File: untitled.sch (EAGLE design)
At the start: 49 parts, among them J2 1x3 RA Female .1", J3 CORTEX_DEBUG_PTH, J4 USB-MICROB, Q1 BSS123

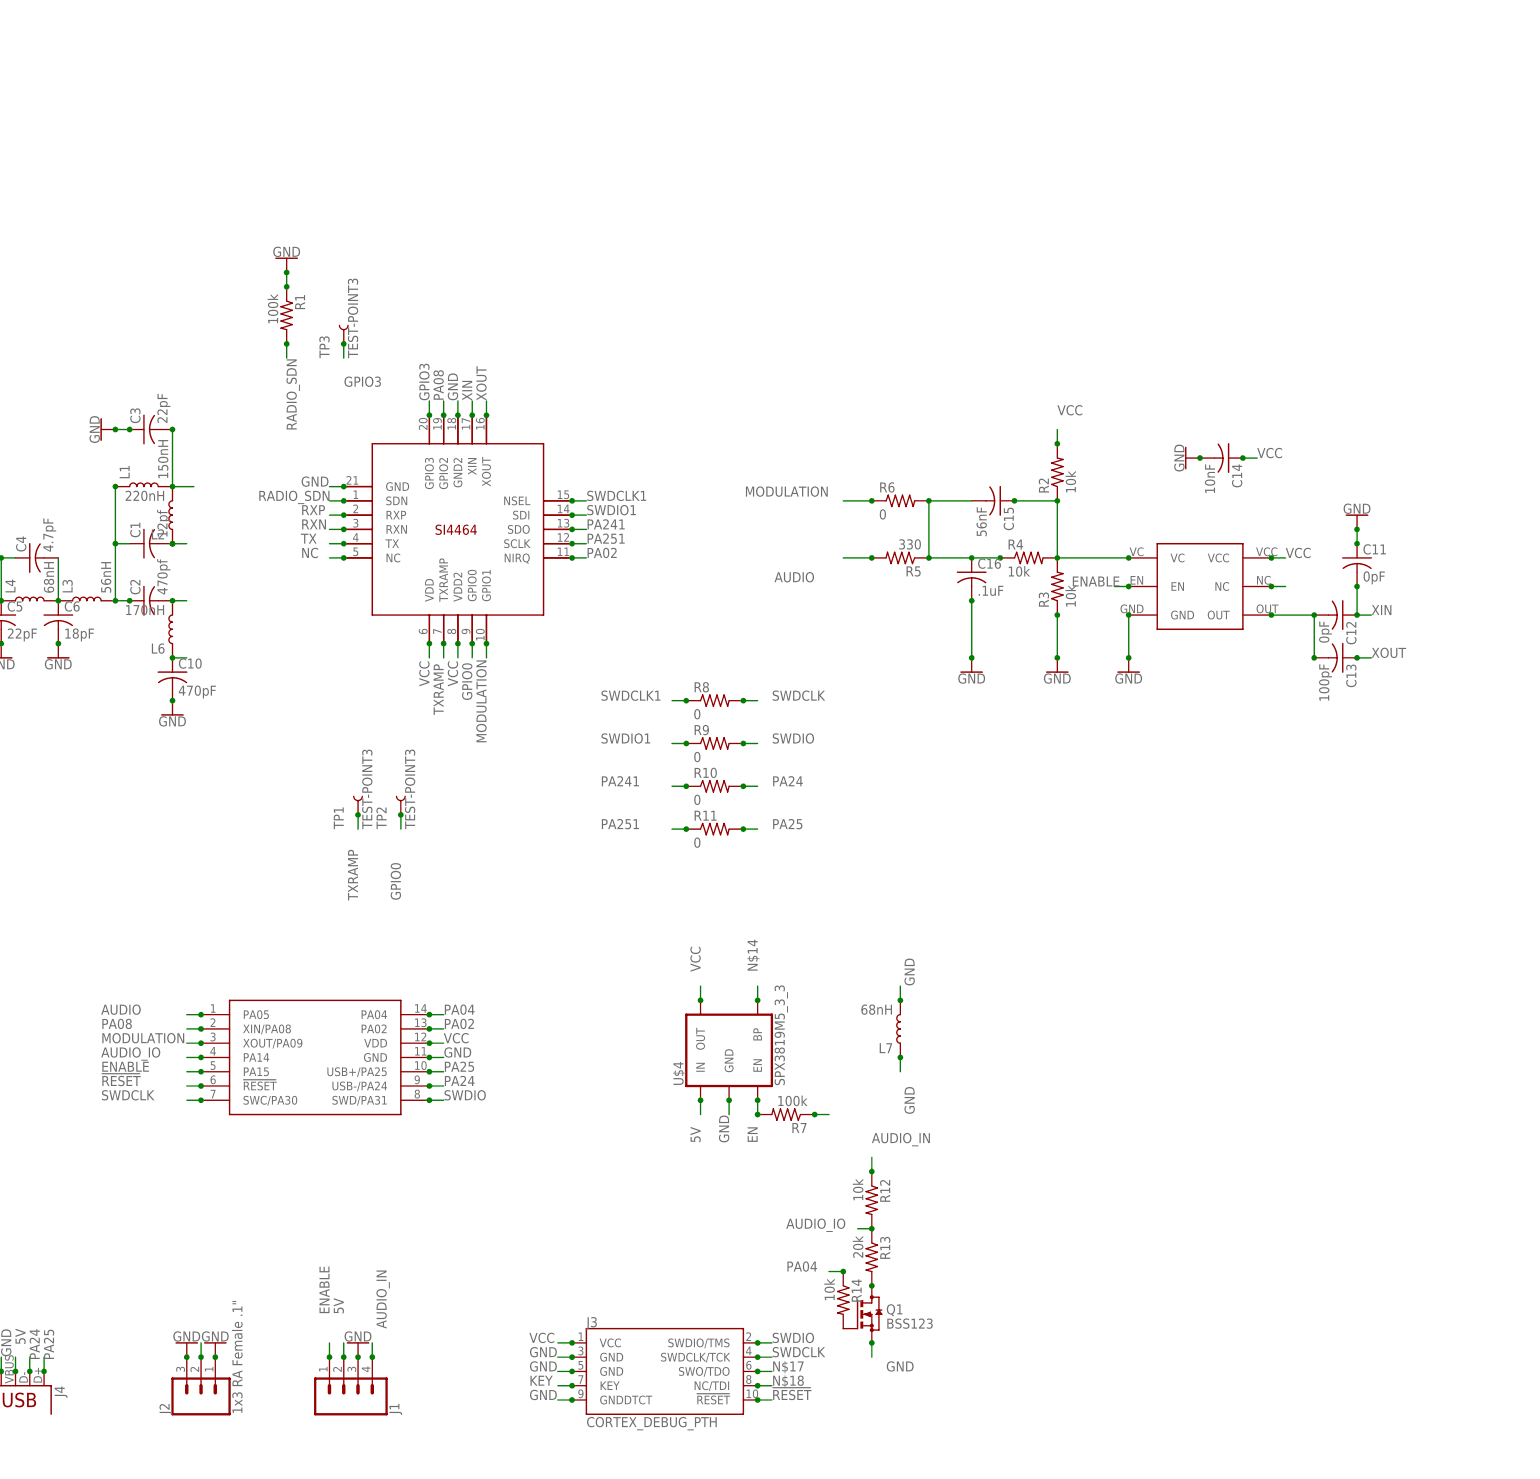
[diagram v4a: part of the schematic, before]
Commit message: changed audio input path
changed audio input to make the samd11c14 decode the audio and resend it to the VCO. Added fets to allow for i2c over enable and audio pins for future use.
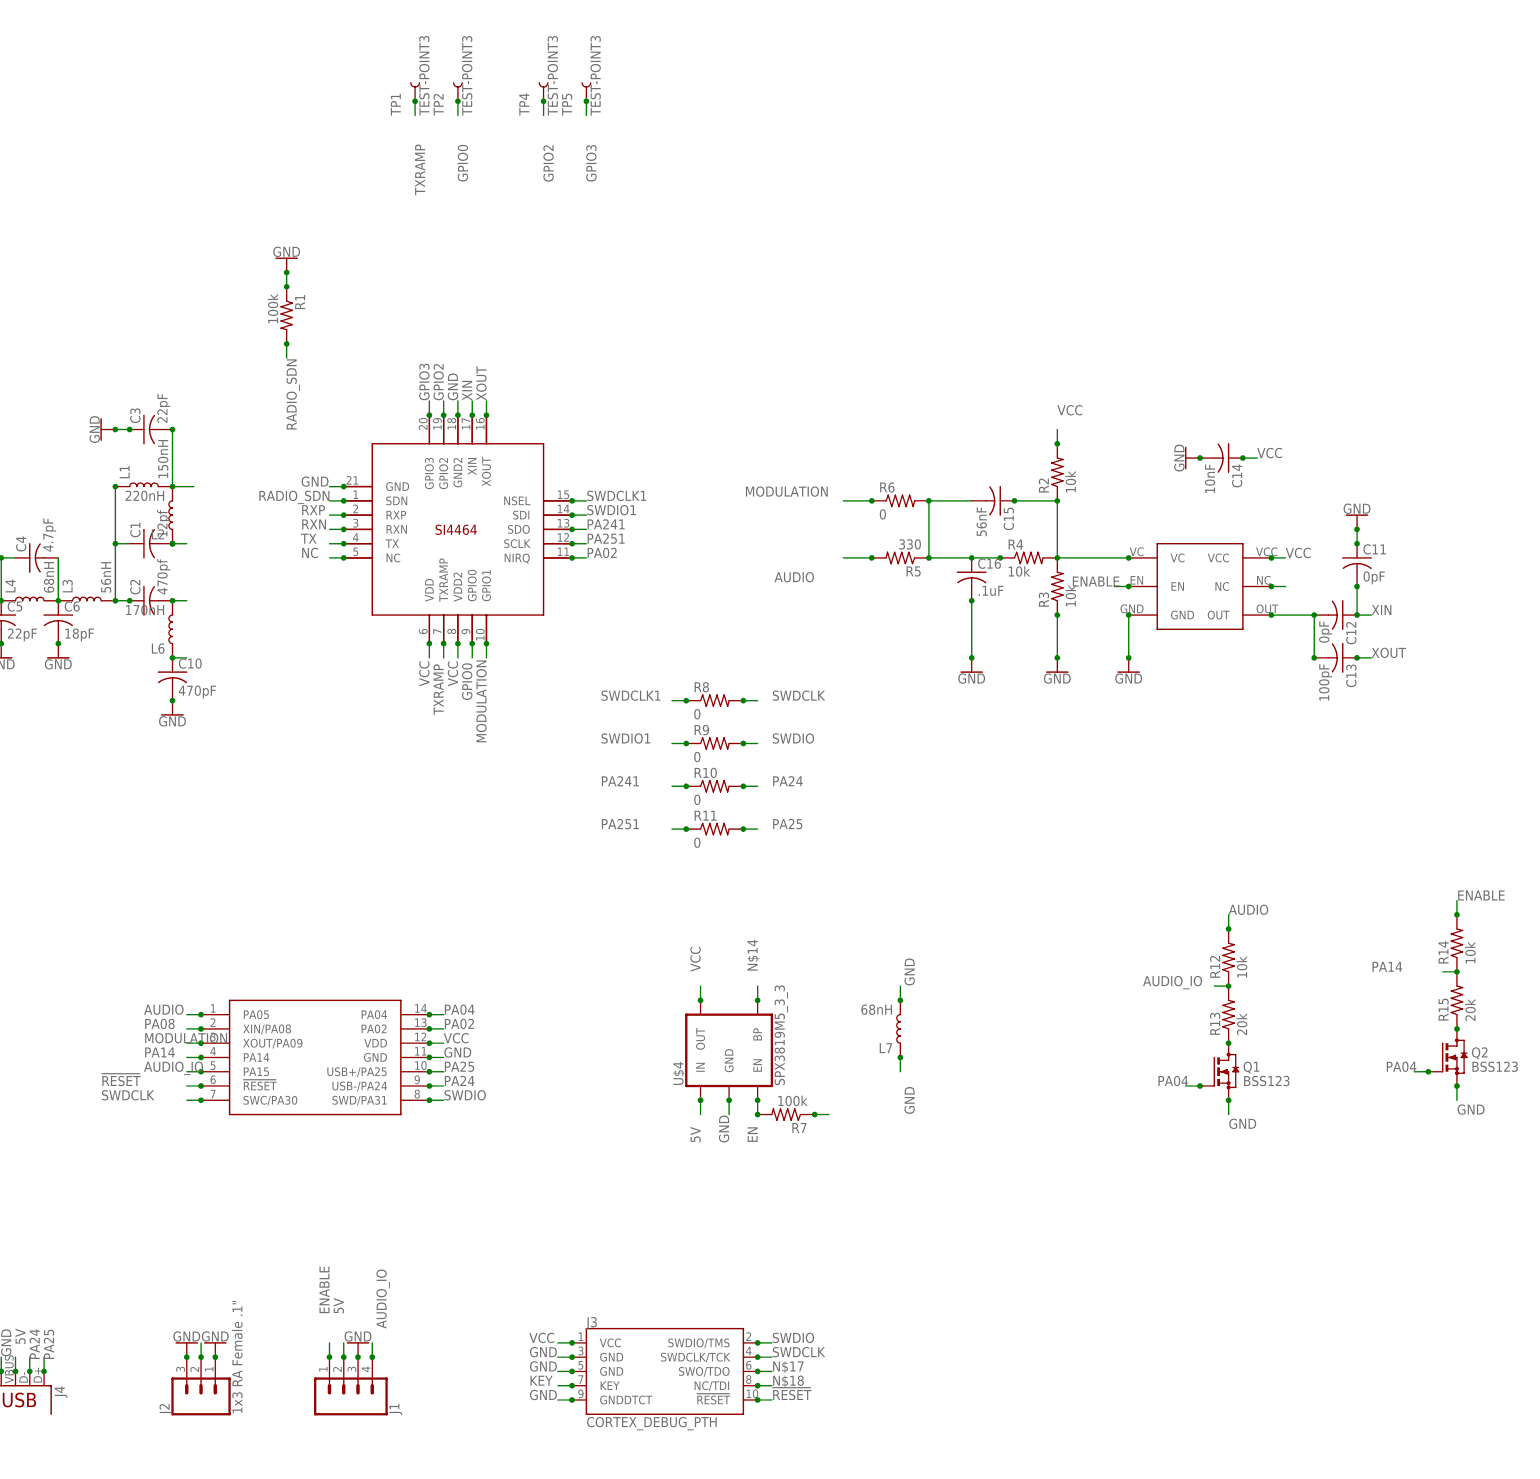
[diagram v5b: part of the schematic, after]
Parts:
- removed TP3: TEST-POINT3, SparkFun-Connectors:TEST-POINT3
- added Q2: BSS123, transistor-small-signal:BSS123
- added R15: 20k, resistor:R-US_R0402
- added TP4, TP5: TEST-POINT3, SparkFun-Connectors:TEST-POINT3
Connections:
- removed net AUDIO_IN: J1.4, R12.1
- new net GPIO2: TP4.1, U$2.GPIO2
- new net PA14: R14.1, R15.2, U$3.PA14
- net AUDIO: now also R12.2
- net AUDIO_IO: now also J1.4, R12.1, R13.2, U$3.PA15; no longer R12.2, R13.1, U$3.PA14
- net ENABLE: now also R14.2; no longer U$3.PA15
- net GND: now also Q2.S
- net GPIO3: now also TP5.1; no longer TP3.1
- net N$7: now also R13.1; no longer R13.2
- net N$8: now also Q2.D, R15.1; no longer Q1.G, R14.2
- net PA04: now also Q1.G, Q2.G; no longer R14.1
- net PA08: no longer U$2.GPIO2
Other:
- moved on the sheet: Q1, R12, R13, R14, TP1, TP2

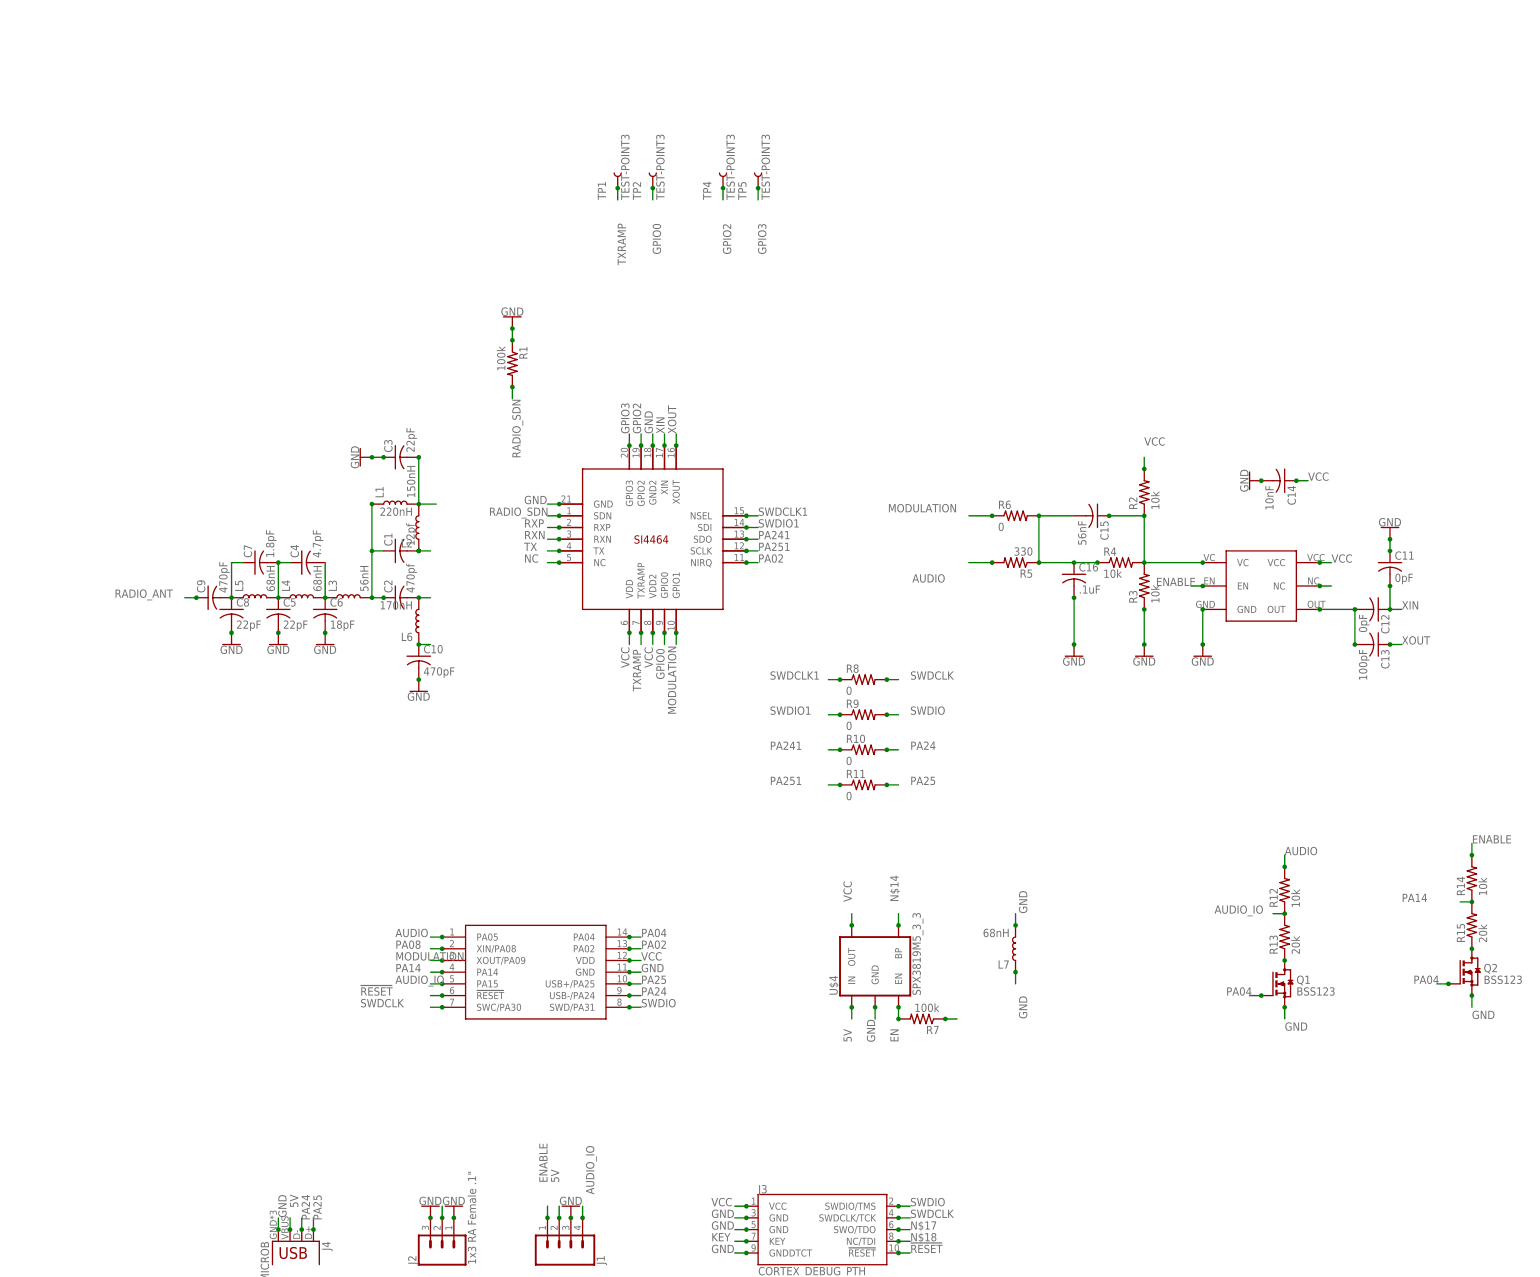
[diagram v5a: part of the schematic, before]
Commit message: RC1
added 0805 resistor divider package for voltage level conversion of inputs. Final routing pass and verified DRC.
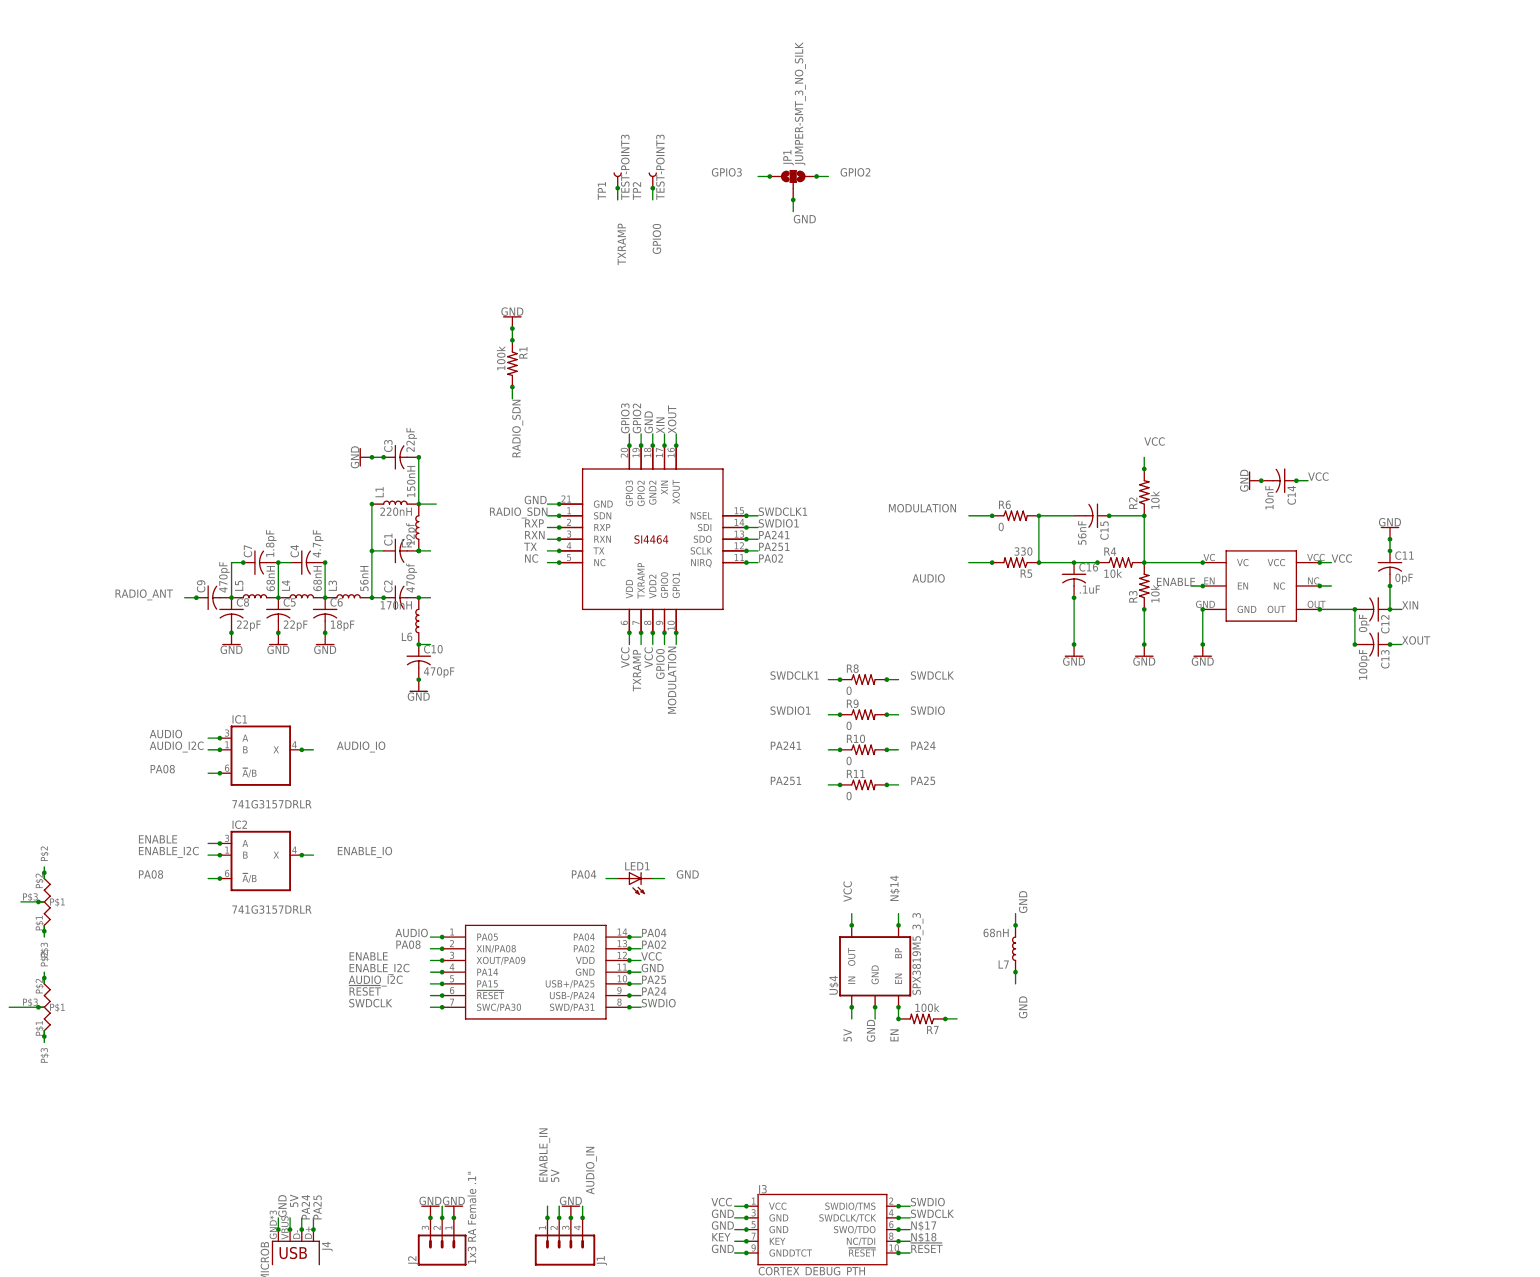
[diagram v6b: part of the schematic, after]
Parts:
- removed Q1, Q2: BSS123, transistor-small-signal:BSS123
- removed R12, R14: 10k, resistor:R-US_R0402
- removed R13, R15: 20k, resistor:R-US_R0402
- removed TP4, TP5: TEST-POINT3, SparkFun-Connectors:TEST-POINT3
- added IC1, IC2: 741G3157DRLR, 74xx-little-us:741G3157DRLR
- added JP1: JUMPER-SMT_3_NO_SILK, SparkFun-Jumpers:JUMPER-SMT_3_NO_SILK
- added LED1: (no value), adafruit:LEDCHIP-LED0603
- added U$5, U$6: RM20A10K/20K, resistor:RM20A10K/20K
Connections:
- removed net N$7: Q1.D, R13.1
- removed net N$8: Q2.D, R15.1
- removed net PA14: R14.1, R15.2, U$3.PA14
- new net AUDIO_I2C: IC1G$1.B, U$3.PA15
- new net AUDIO_IN: J1.4, U$6.P$3
- new net ENABLE_I2C: IC2G$1.B, U$3.PA14
- new net ENABLE_IN: J1.1, U$5.P$3
- new net ENABLE_IO: IC2G$1.X, U$5.P$1
- net AUDIO: now also IC1G$1.A; no longer R12.2
- net AUDIO_IO: now also IC1G$1.X, U$6.P$1; no longer J1.4, R12.1, R13.2, U$3.PA15
- net ENABLE: now also IC2G$1.A, U$3.XOUT/PA09; no longer J1.1, R14.2
- net GND: now also JP1.2, LED1.C, U$5.P$2, U$6.P$2; no longer Q1.S, Q2.S
- net GPIO2: now also JP1.3; no longer TP4.1
- net GPIO3: now also JP1.1; no longer TP5.1
- net MODULATION: no longer U$3.XOUT/PA09
- net PA04: now also LED1.A; no longer Q1.G, Q2.G
- net PA08: now also IC1G$1.!A!/B, IC2G$1.!A!/B

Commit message: Updated pin placements
updated pin placements to their correct locations. Moved the ti switch to clear the 10 pin jtag header. adjusted board outline to correct size.
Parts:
- added R12, R13: 10k, resistor:R-US_R0402
- added U$7: RADIOMETRIX-HX1, Ava:RADIOMETRIX-HX1
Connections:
- net GPIO2: now also R13.2
- net GPIO3: now also R12.2
- net VCC: now also R12.1, R13.1
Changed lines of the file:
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@@
 <?xml version="1.0" encoding="utf-8"?>
 <!DOCTYPE eagle SYSTEM "eagle.dtd">
-<eagle version="8.6.0">
+<eagle version="8.7.0">
 <drawing>
 <settings>
@@
 <part name="U$5" library="resistor" deviceset="RM20A10K/20K" device=""/>
 <part name="U$6" library="resistor" deviceset="RM20A10K/20K" device=""/>
+<part name="R12" library="resistor" library_urn="urn:adsk.eagle:library:348" deviceset="R-US_" device="R0402" package3d_urn="urn:adsk.eagle:package:26058/1" value="10k"/>
+<part name="R13" library="resistor" library_urn="urn:adsk.eagle:library:348" deviceset="R-US_" device="R0402" package3d_urn="urn:adsk.eagle:package:26058/1" value="10k"/>
+<part name="U$7" library="Ava" deviceset="RADIOMETRIX-HX1" device=""/>
 </parts>
 <sheets>
@@
 <instance part="U$5" gate="G$1" x="-231.14" y="81.28"/>
 <instance part="U$6" gate="G$1" x="-231.14" y="104.14"/>
+<instance part="R12" gate="G$1" x="-73.66" y="266.7" rot="R270"/>
+<instance part="R13" gate="G$1" x="-63.5" y="266.7" rot="R270"/>
+<instance part="U$7" gate="G$1" x="53.34" y="106.68"/>
 </instances>
 <busses>
@@
 <junction x="-63.5" y="261.62"/>
 <label x="-58.42" y="261.62" size="1.778" layer="95"/>
+<pinref part="R13" gate="G$1" pin="2"/>
 </segment>
 </net>
@@
 <junction x="-73.66" y="261.62"/>
 <label x="-86.36" y="261.62" size="1.778" layer="95"/>
+<pinref part="R12" gate="G$1" pin="2"/>
 </segment>
 </net>
@@
 <label x="-55.88" y="104.14" size="1.778" layer="95" rot="R90"/>
 </segment>
-</net>
+<segment>
+<pinref part="R12" gate="G$1" pin="1"/>
+<wire x1="-73.66" y1="271.78" x2="-73.66" y2="274.32" width="0.1524" layer="91"/>
+<junction x="-73.66" y="271.78"/>
+</segment>
+<segment>
+<pinref part="R13" gate="G$1" pin="1"/>
+<wire x1="-63.5" y1="271.78" x2="-63.5" y2="274.32" width="0.1524" layer="91"/>
+<junction x="-63.5" y="271.78"/>
+</segment>
+</net>
